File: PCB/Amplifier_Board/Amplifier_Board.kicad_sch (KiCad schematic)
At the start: 35 parts, among them J1 Conn_01x04_Pin, J2 Conn_01x10_Pin, J3 Conn_01x08_Pin, J4 Conn_01x08_Pin, J5 Conn_01x02_Pin, U1 ADA8282, U2 ADA8282

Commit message: Worked on PCB V2 and Added Instrumentation Amp test data
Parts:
- C13, C14, C16, C19: value 2.2u -> 22u
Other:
- note added: "INPUT IMPEDANCE OF EACH DIFFERENTIAL PIN IS 785 Ohms SO 22uF CAP CREATES HPF WITH CUTOFF AT 9.2 Ohms"
- note added: "INPUTS ARE AC COUPLED AND BIASED TO 1/2 AVDD (3V3) SO INPUTS CAN HAVE A MAX SWING FROM 0 - 3V3"
- moved on the sheet: C1, C10, C11, C12, C13, C14, C15, C16, C17, C18, C19, C2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

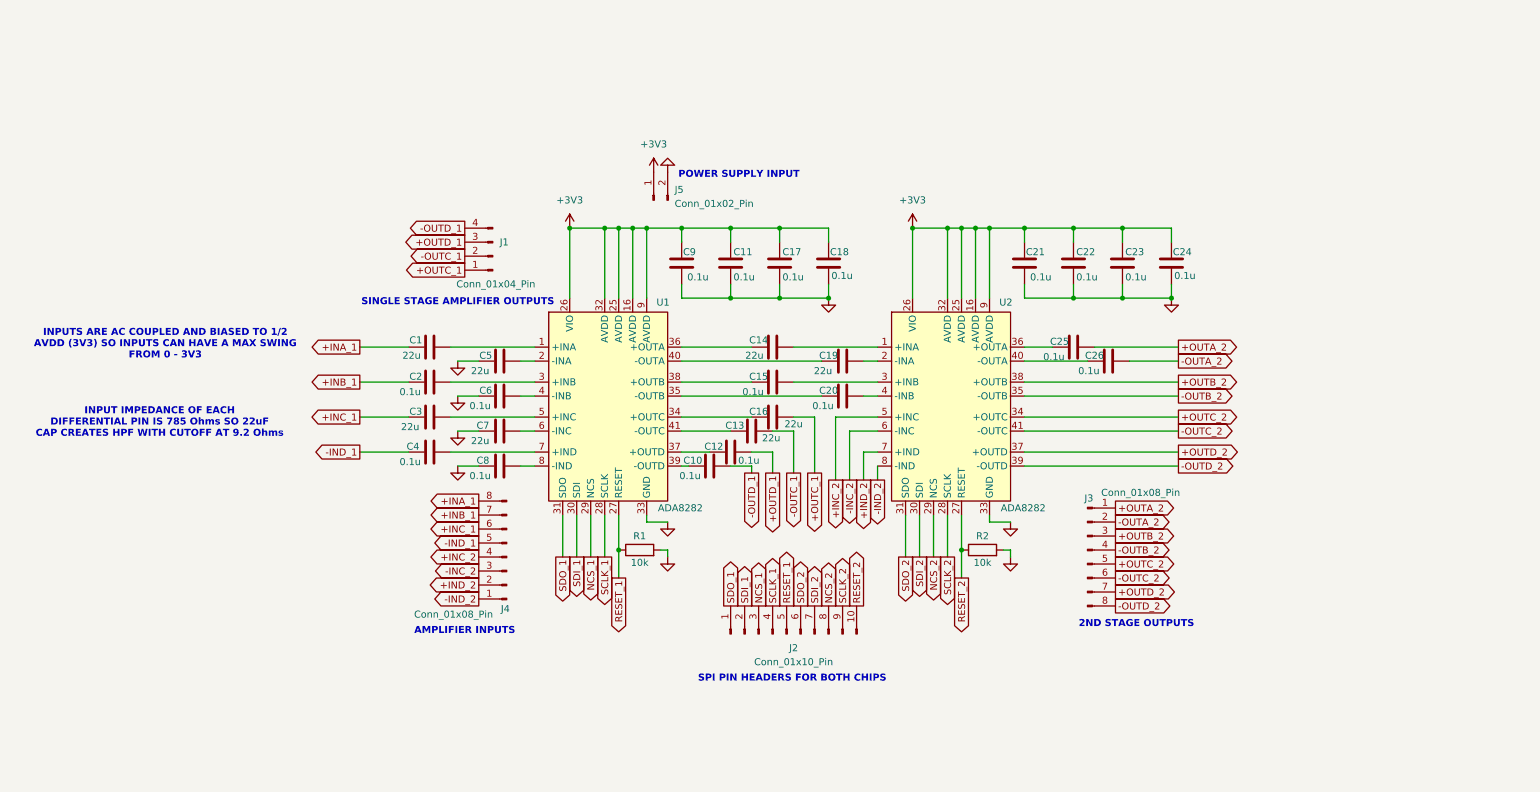
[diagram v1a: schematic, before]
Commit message: Updated File Layout
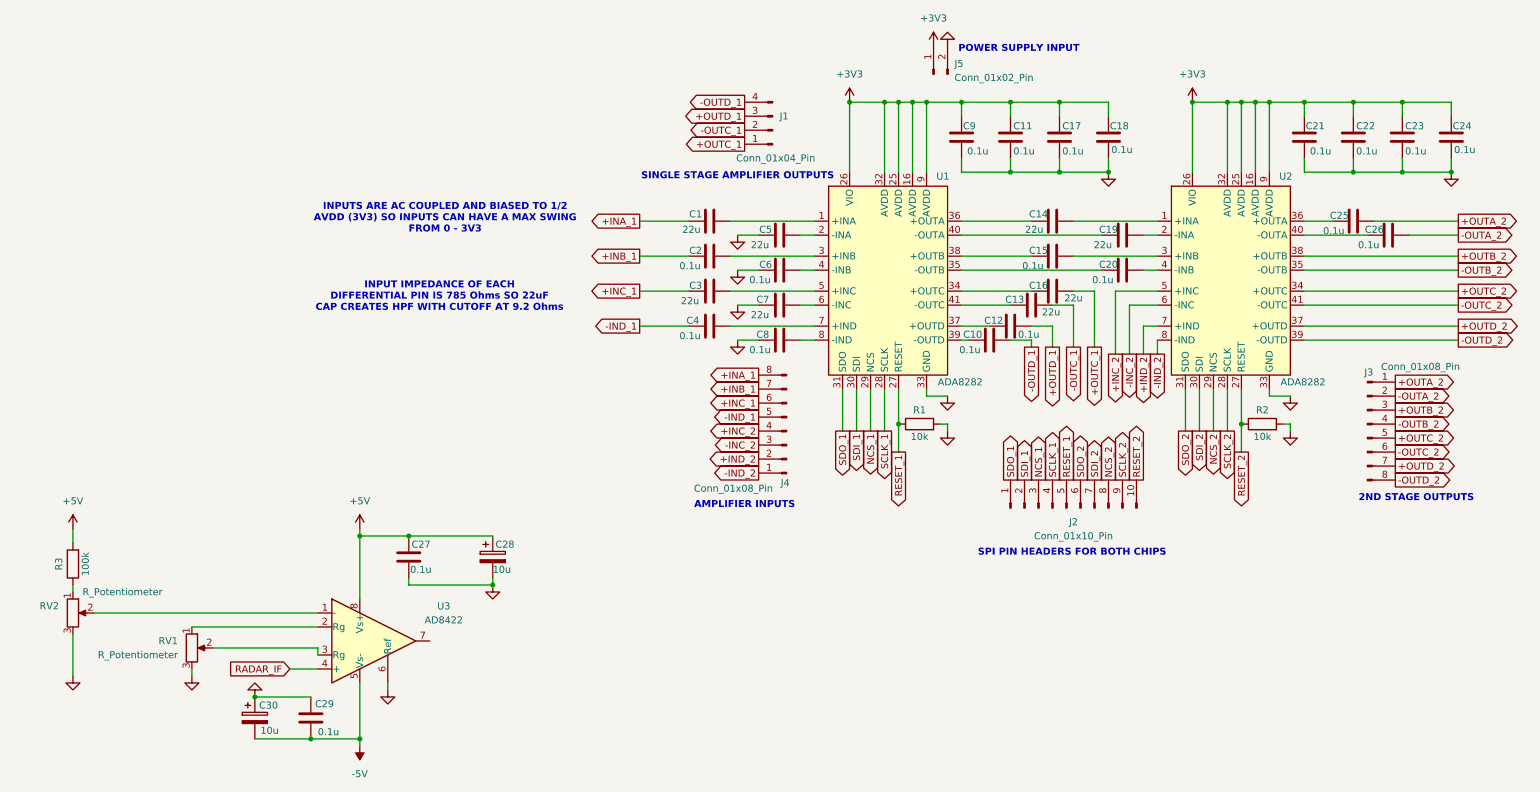
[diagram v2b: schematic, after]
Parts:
- added C27, C29: 0.1u, symbol Device:C
- added C28, C30: 10u, symbol Device:C_Polarized
- added R3: 100k, symbol Device:R
- added RV1, RV2: R_Potentiometer, symbol Device:R_Potentiometer
- added U3: AD8422, symbol Amplifier_Instrumentation:AD8422
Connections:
- net GND: now also C27.2, C28.2, C29.1, C30.1, RV1.3, RV2.3, U3.6 (Ref)
- new net: R3.1, RV2.1
- new net: RV2.2, U3.1 (-)
- new net: RV1.1, U3.2 (Rg)
- new net: RV1.2, U3.3 (Rg)
- new net +5V: C27.1, C28.1, R3.2, U3.8 (Vs+)
- new net -5V: C29.2, C30.2, U3.5 (Vs-)
- new net RADAR_IF: U3.4 (+)
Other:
- company: (none) -> Author: Mishay Naidoo
- moved on the sheet: C1, C10, C11, C12, C13, C14, C15, C16, C17, C18, C19, C2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
